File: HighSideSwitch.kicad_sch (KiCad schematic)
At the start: 22 parts, among them J1 Conn_02x02_Odd_Even, Q1 CSD18540Q5B, Q2 8050, Q3 8050, U1 BTS443P, U2 LM5050-1

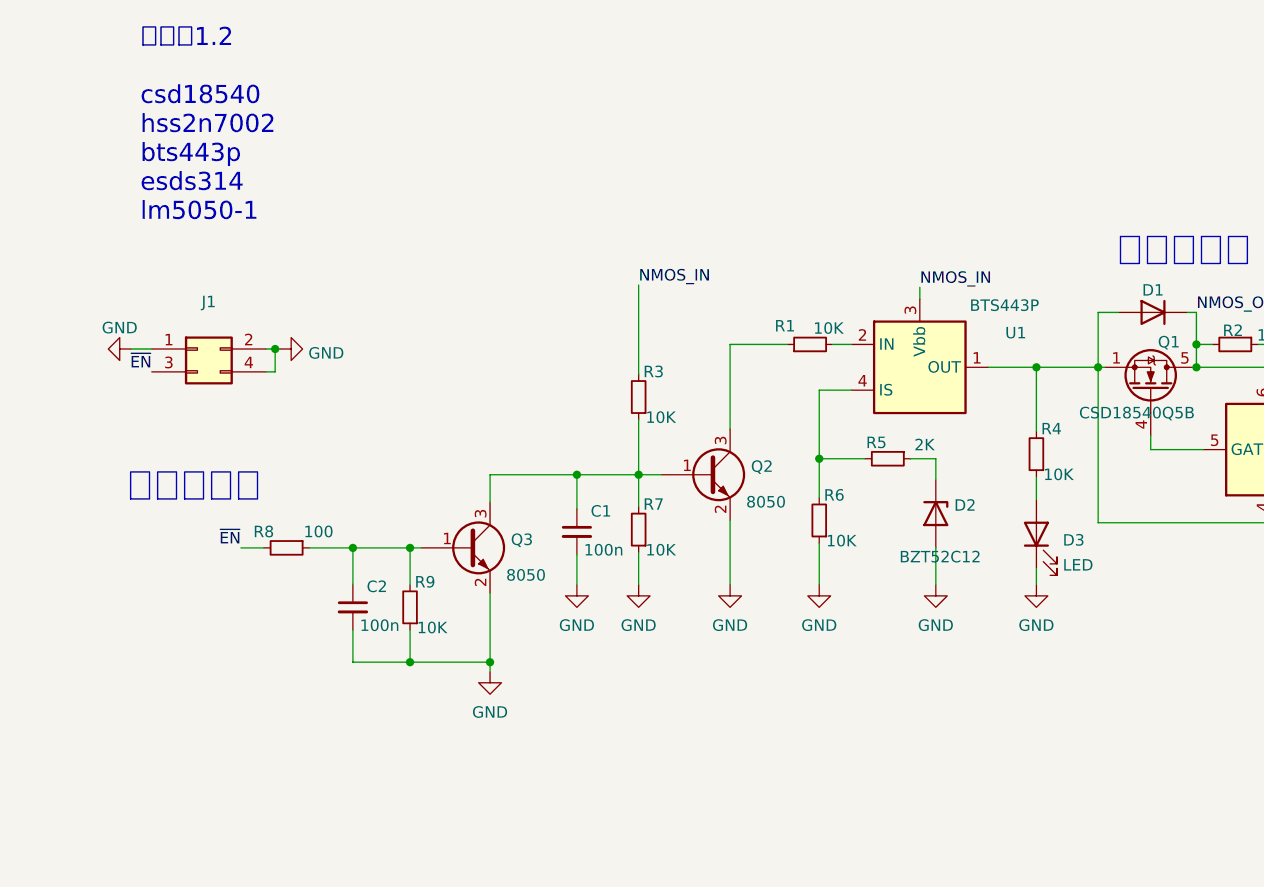
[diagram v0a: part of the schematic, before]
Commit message: Use LM5060 as high side switch instead BTS443P
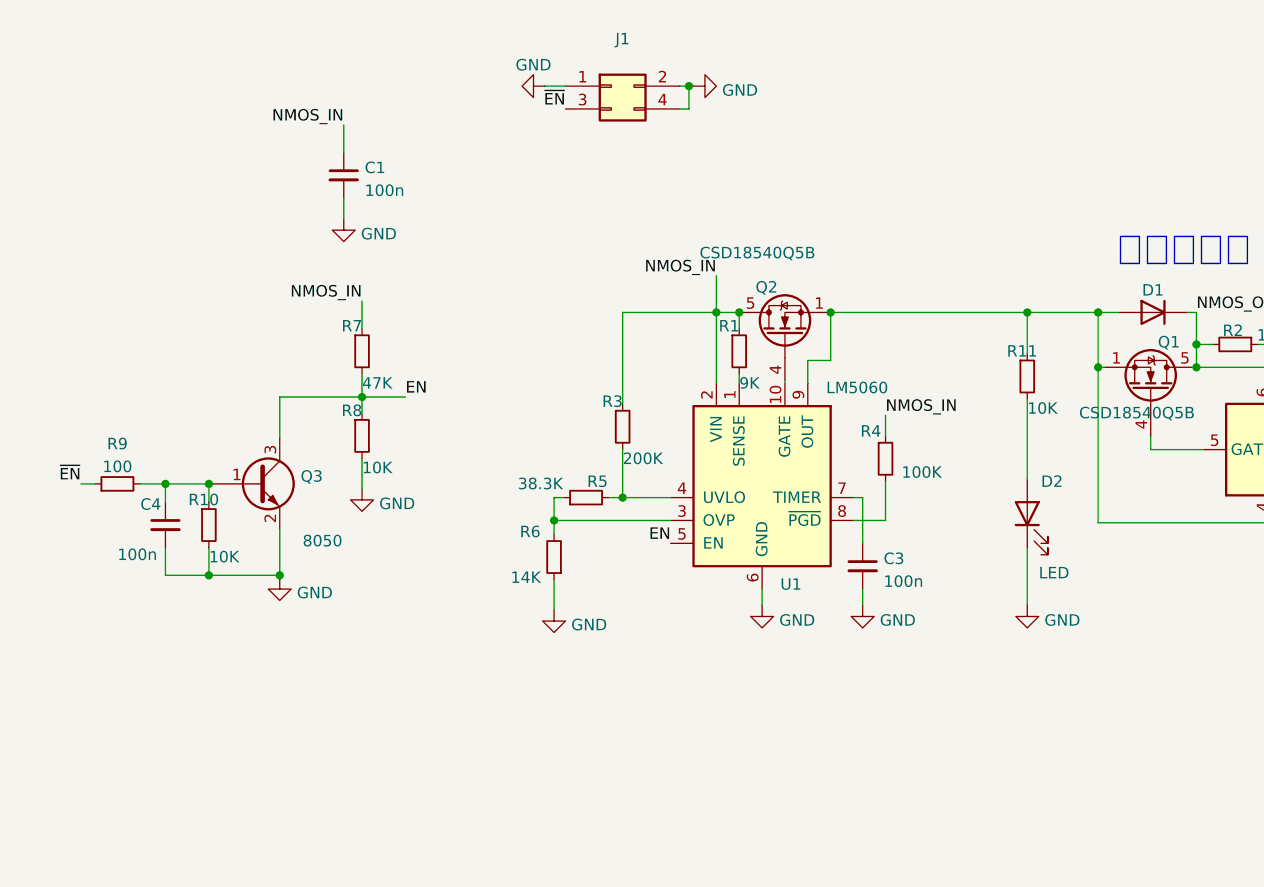
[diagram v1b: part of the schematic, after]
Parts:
- removed C2: 100n, Capacitor_SMD:C_0402_1005Metric, symbol Device:C_Small
- removed D2: BZT52C12, Diode_SMD:D_SOD-123, symbol Diode:BZT52Bxx
- removed D3: LED, LED_SMD:LED_0603_1608Metric, symbol Device:LED
- removed Q2: 8050, Package_TO_SOT_SMD:SOT-23, symbol Device:Q_NPN_BEC
- removed U1: BTS443P, Package_TO_SOT_SMD:TO-252-4, symbol Power_Management:BTS443P
- added C3, C4: 100n, Capacitor_SMD:C_0402_1005Metric, symbol Device:C_Small
- added D2: LED, LED_SMD:LED_0603_1608Metric, symbol Device:LED
- added Q2: CSD18540Q5B, Package_TO_SOT_SMD:TDSON-8-1, symbol Transistor_FET:CSD18540Q5B
- added R10, R11: 10K, Resistor_SMD:R_0402_1005Metric, symbol Device:R_Small
- added U1: LM5060, Package_SO:MSOP-10_3x3mm_P0.5mm, symbol Power_Management:LM5060
- Q3: footprint Package_TO_SOT_SMD:SOT-23 -> Package_TO_SOT_SMD:TSOT-23
- R1: value 10K -> 9K
- R3: value 10K -> 200K
- R4: value 10K -> 100K; footprint Resistor_SMD:R_0603_1608Metric -> Resistor_SMD:R_0402_1005Metric
- R5: value 2K -> 38.3K
- R6: value 10K -> 14K
- R7: value 10K -> 47K
- R8: value 100 -> 10K
- R9: value 10K -> 100
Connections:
- net GND: now also R8.2, C3.2, C4.2, D2.1 (K), R10.2, U1.6 (GND); no longer R7.1, R9.1
- net NMOS_IN: now also C1.1, R1.1, R3.1, R4.1, R7.1, Q2.5 (D), U1.2 (VIN); no longer R3.2
- net ~{EN}: now also R9.1; no longer R8.2
- net at Q3.1 (B), R9.2: now also C4.1, R10.1; no longer R8.1
- net EN: now reaches Q3.3 (C), R7.2
- net EN: now also R8.1, U1.5 (EN); no longer C1.1, R3.1
- net at R6.2: now also R5.1, U1.3 (OVP); no longer R5.2
- net at D1.1 (A), D1.2 (A), Q1.1 (S)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: now also Q2.1 (S), Q2.2 (S), Q2.3 (S), R11.1, U1.9 (OUT); no longer R4.2
- net at R1.2: now also U1.1 (SENSE)
- new net: Q2.4 (G), U1.10 (GATE)
- new net: R3.2, R5.2, U1.4 (UVLO)
- new net: C3.1, U1.7 (TIMER)
- new net: R4.2, U1.8 (~{PGD})
- new net: D2.2 (A), R11.2
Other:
- note removed: "低电平有效"
- note removed: "板厚：1.2 csd18540 hss2n7002 bts443p esds314 lm5050-1"
- moved on the sheet: J1

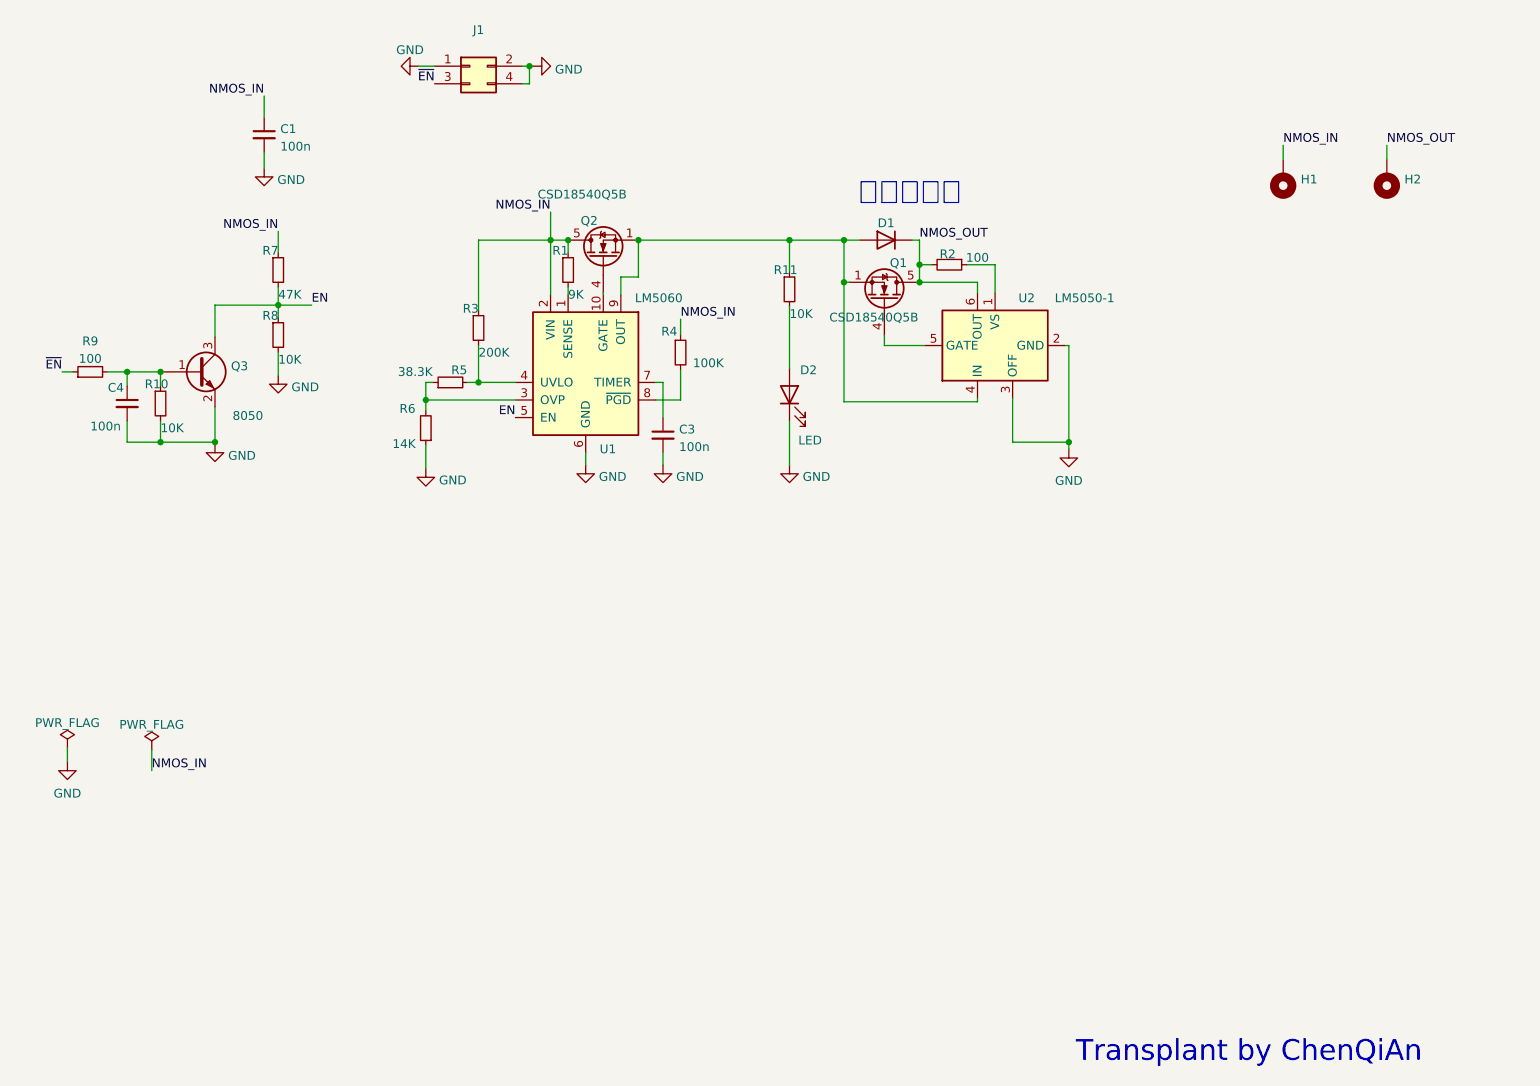
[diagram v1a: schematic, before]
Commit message: Complete ORing MOSFET
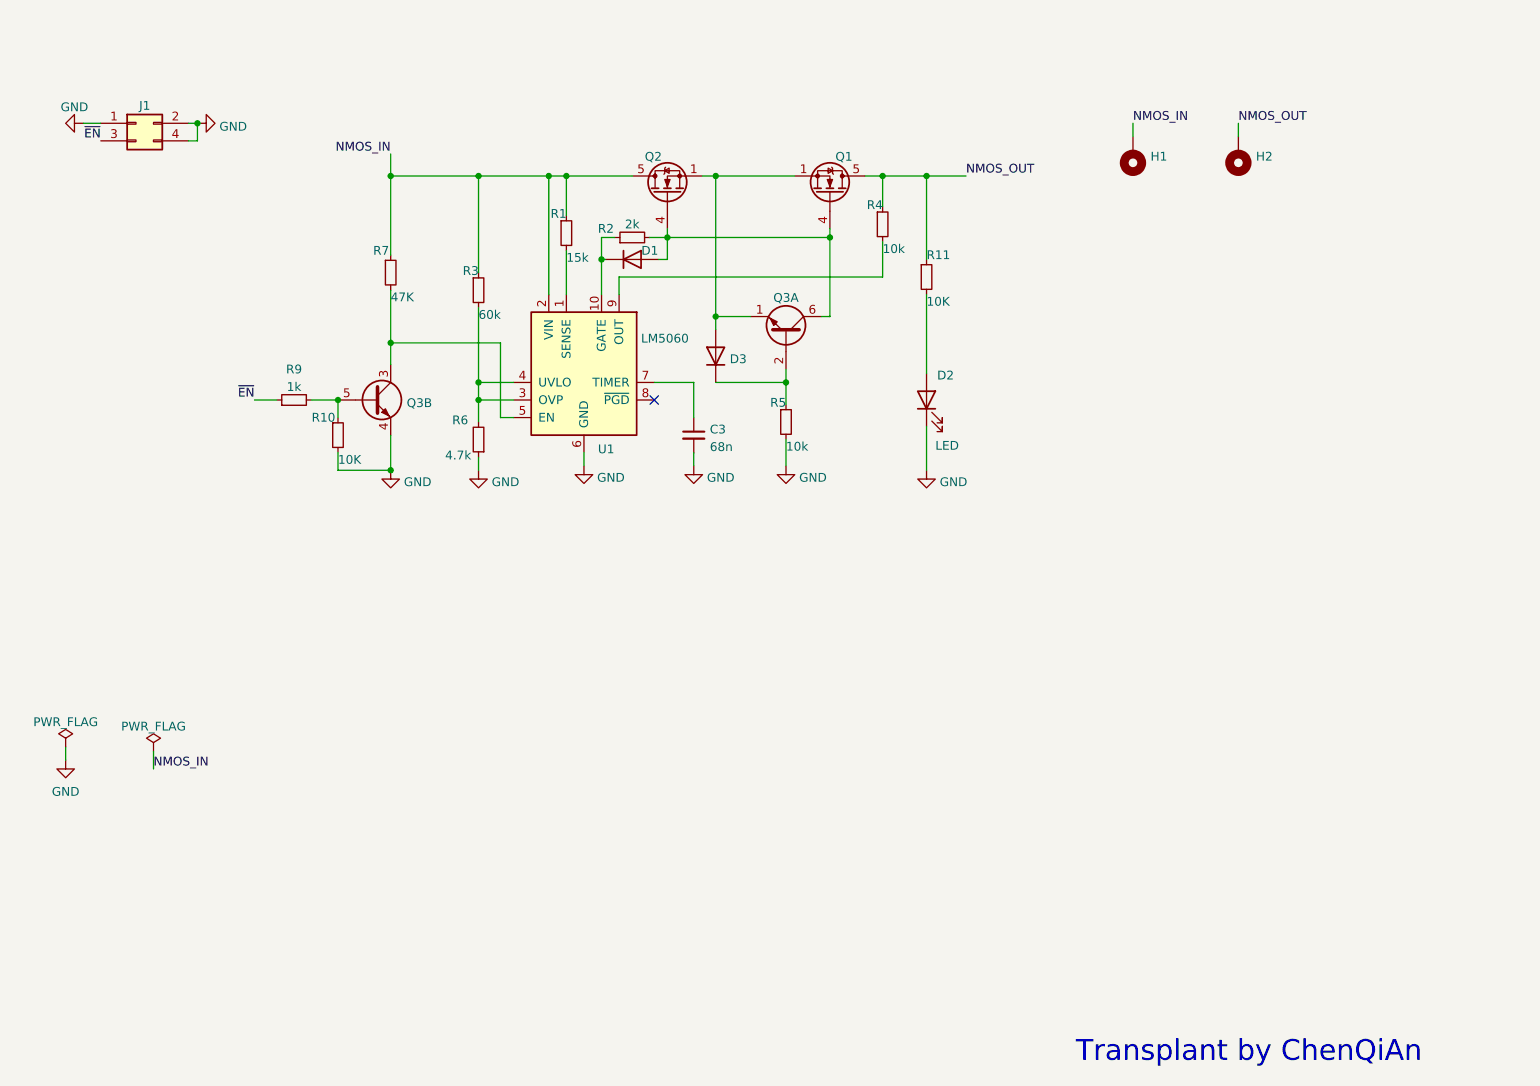
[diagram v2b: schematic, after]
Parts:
- removed C1, C4: 100n, Capacitor_SMD:C_0402_1005Metric, symbol Device:C_Small
- removed D1: VS-6ESU06, Package_TO_SOT_SMD:TO-277A, symbol Diode:VS-6ESU06
- removed Q3: 8050, Package_TO_SOT_SMD:TSOT-23, symbol Device:Q_NPN_BEC
- removed R8: 10K, Resistor_SMD:R_0402_1005Metric, symbol Device:R_Small
- removed U2: LM5050-1, Package_TO_SOT_SMD:TSOT-23-6, symbol Power_Management:LM5050-1
- added D1, D3: 1N4001, Diode_SMD:D_SOD-323, symbol Diode:1N4001
- added Q3: Q_Dual_NPN_NPN_E1B1C2E2B2C1, Package_TO_SOT_SMD:SOT-363_SC-70-6, symbol Device:Q_Dual_NPN_NPN_E1B1C2E2B2C1
- C3: value 100n -> 68n
- R1: value 9K -> 15k
- R2: value 100 -> 2k
- R3: value 200K -> 60k
- R4: value 100K -> 10k
- R5: value 38.3K -> 10k
- R6: value 14K -> 4.7k
- R9: value 100 -> 1k
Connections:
- net GND: now also R5.2, Q3.4 (E2)
- net NMOS_IN: no longer R4.1
- net NMOS_OUT: now also R11.1, R4.1; no longer R2.2
- net at R10.1, R9.2: now also Q3.5 (B2)
- net at R2.1: now also U1.10 (GATE), D1.1 (K)
- net at Q2.4 (G): now also Q1.4 (G), R2.2, D1.2 (A), Q3.6 (C1); no longer U1.10 (GATE)
- net at R6.2, U1.3 (OVP): now also R3.2, U1.4 (UVLO); no longer R5.1
- net at U1.8 (~{PGD}): no longer R4.2
- net at Q1.1 (S), Q1.2 (S), Q1.3 (S)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: now also D3.2 (A), Q3.1 (E1); no longer R11.1, U1.9 (OUT)
- net EN: no longer names the net of R7.2, U1.5 (EN)
- net EN: now also Q3.3 (C2)
- new net: R4.2, U1.9 (OUT)
- new net: D3.1 (K), Q3.2 (B1), R5.1
- no-connect marks 0 -> 1
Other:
- note removed: "理想二极管"
- moved on the sheet: C3, D2, H1, H2, J1, Q2, R1, R10, R11, R3, R6, R7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
